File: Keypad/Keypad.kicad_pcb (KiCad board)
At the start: 2 copper layers, 41 parts, among them SW1 SW_Push, SW10 SW_Push, SW11 SW_Push, SW12 SW_Push, SW13 SW_Push, SW14 SW_Push, SW15 SW_Push, SW16 SW_Push, SW2 SW_Push, SW3 SW_Push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

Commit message: Working on de10lite keypad 2.0
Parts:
- removed R6_1K, R7_1K, R8_1K: R_Small_US, Resistor_THT:R_Axial_DIN0207_L6.3mm_D2.5mm_P7.62mm_Horizontal
- added R6_1K1: R_Small_US, Resistor_SMD:R_0603_1608Metric, F.Cu at (113.2, 66.5)
- added R7_1K1: R_Small_US, Resistor_SMD:R_0603_1608Metric, F.Cu at (113.2, 77.5)
- added R8_1K1: R_Small_US, Resistor_SMD:R_0603_1608Metric, F.Cu at (113.2, 87.8)
- D1, D10, D11, D12, D13, D14, D15, D16, D2, D3, D4, D5, D6, D7, D8, D9: footprint Diode_THT:D_A-405_P7.62mm_Horizontal -> Diode_SMD:D_SOD-123
- R1_330, R2_330, R3_330, R4_330: footprint Resistor_THT:R_Axial_DIN0207_L6.3mm_D2.5mm_P7.62mm_Horizontal -> Resistor_SMD:R_0603_1608Metric
- R5_1K1: renamed from R5_1K; footprint Resistor_THT:R_Axial_DIN0207_L6.3mm_D2.5mm_P7.62mm_Horizontal -> Resistor_SMD:R_0603_1608Metric
- SW1, SW10, SW11, SW12, SW13, SW14, SW15, SW16, SW2, SW3, SW4, SW5, SW6, SW7, SW8, SW9: footprint Resistor_THT:R_Axial_DIN0204_L3.6mm_D1.6mm_P5.08mm_Horizontal -> Button_Switch_SMD:SW_SPST_TL3305B
- moved D1 4.16 mm to (121.3, 57.4), turned to 180 degrees
- moved R5_1K1 4.10 mm to (113.2, 56.9)
- moved D4 4.00 mm to (121.3, 88.1), turned to 180 degrees
- moved D9 3.95 mm to (142.7, 57.4), turned to 180 degrees
- moved D11 3.91 mm to (143.1, 78.0), turned to 180 degrees
- moved D12 3.88 mm to (143.0, 88.1), turned to 180 degrees
- moved D8 3.88 mm to (132.2, 88.1), turned to 180 degrees
- moved D13 3.86 mm to (153.7, 57.5), turned to 180 degrees
- moved D2 3.84 mm to (121.4, 67.9), turned to 180 degrees
- moved D5 3.81 mm to (132.0, 57.4), turned to 180 degrees
- moved D3 3.79 mm to (121.3, 78.0), turned to 180 degrees
- moved D10 3.79 mm to (142.9, 67.9), turned to 180 degrees
- moved D14 3.79 mm to (153.7, 67.9), turned to 180 degrees
- moved D7 3.79 mm to (132.2, 78.0), turned to 180 degrees
- moved D16 3.75 mm to (153.7, 88.1), turned to 180 degrees
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- renumbered Keypad to U1
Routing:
- net Net-(SW13-Pad2): track 47.7 -> 90.1 mm, vias 0 -> 4
- net Net-(SW1-Pad2): track 58.4 -> 97.9 mm, vias 0 -> 4
- net Net-(SW10-Pad2): track 45.2 -> 82.3 mm, vias 0 -> 4
- net Net-(SW5-Pad2): track 52.5 -> 88.3 mm, vias 0 -> 4
- net Net-(D8-Pad1): track 5.11 -> 19.6 mm
- net Net-(D12-Pad1): track 5.10 -> 19.5 mm
- net Net-(D6-Pad1): track 5.30 -> 19.6 mm
- net Net-(D5-Pad1): track 5.38 -> 19.7 mm
- net Net-(D13-Pad1): track 5.54 -> 19.8 mm
- net Net-(D16-Pad1): track 5.05 -> 19.3 mm
- net Net-(D10-Pad1): track 5.38 -> 19.6 mm
- net Net-(D9-Pad1): track 5.44 -> 19.6 mm
- net Net-(D14-Pad1): track 5.48 -> 19.6 mm
- net Net-(D1-Pad1): track 5.18 -> 19.2 mm
- net Net-(D7-Pad1): track 5.63 -> 19.6 mm
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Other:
- board outline added: 54.1 x 54.1 mm
- copper layers 2 -> 4

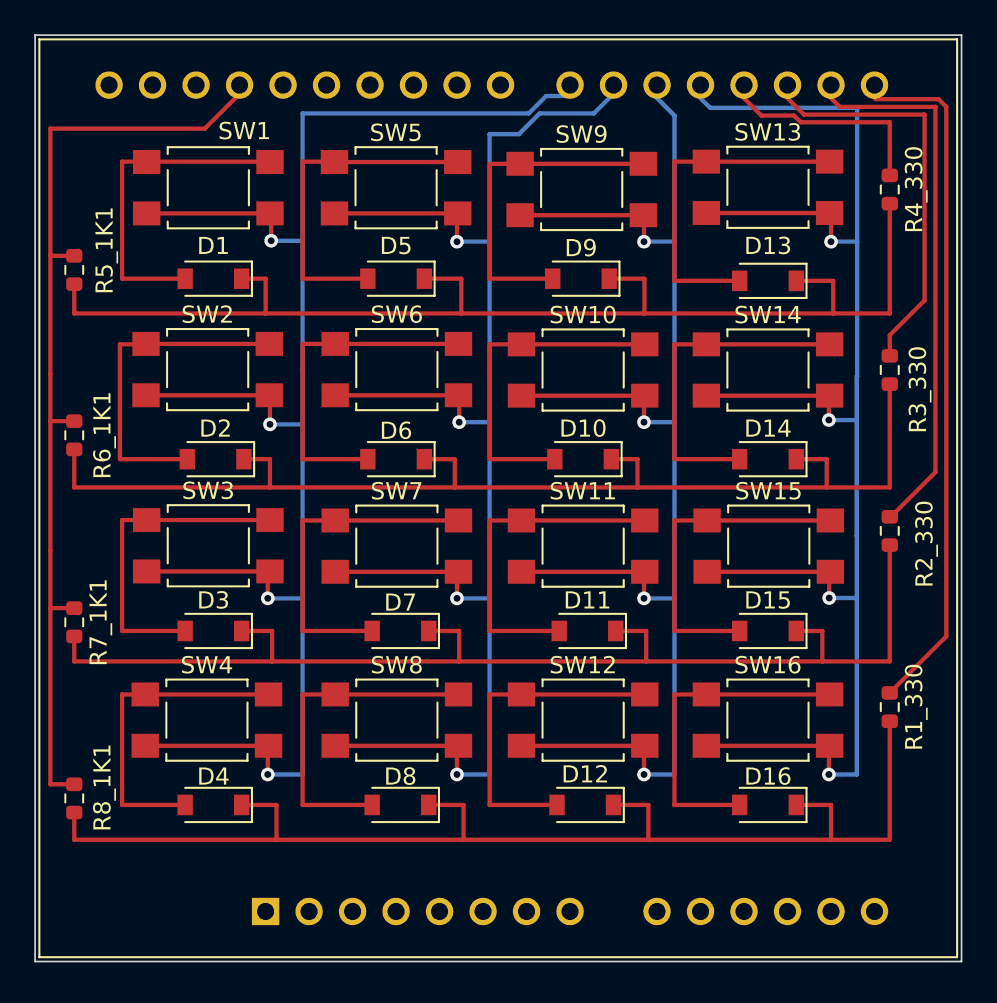
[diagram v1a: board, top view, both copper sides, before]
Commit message: Added in assembly and product files for PCBWay
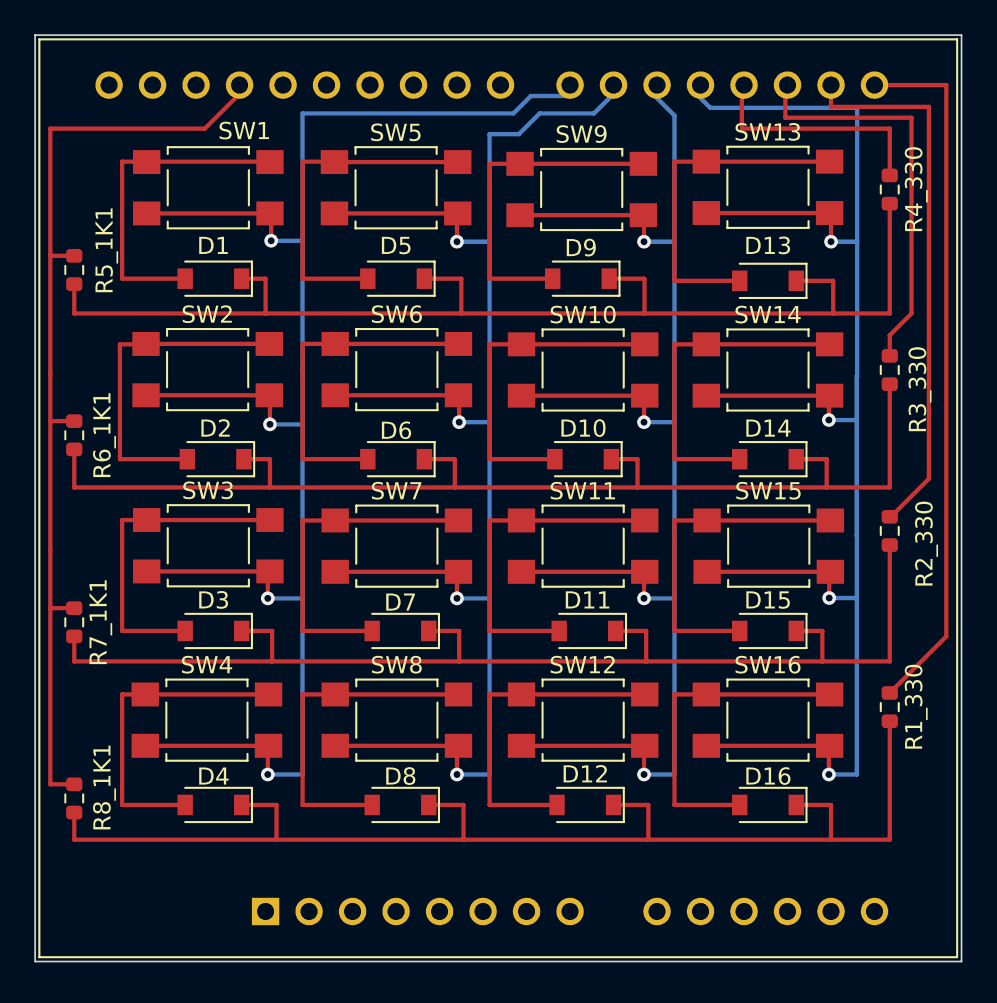
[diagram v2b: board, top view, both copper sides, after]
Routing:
- net Net-(R4_330-Pad1): track 12.3 -> 13.2 mm
- net Net-(R1_330-Pad1): track 40.2 -> 41.1 mm
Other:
- copper layers 4 -> 2
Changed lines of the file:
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@@
 (kicad_pcb (version 20211014) (generator pcbnew)
   (general
-    (thickness 4.69)
+    (thickness 1.6)
   )
   (paper "A4")
   (layers
     (0 "F.Cu" signal)
-    (1 "In1.Cu" signal)
-    (2 "In2.Cu" signal)
     (31 "B.Cu" signal)
     (32 "B.Adhes" user "B.Adhesive")
@@
       (layer "F.Cu" (type "copper") (thickness 0.035))
       (layer "dielectric 1" (type "core") (thickness 1.51) (material "FR4") (epsilon_r 4.5) (loss_tangent 0.02))
-      (layer "In1.Cu" (type "copper") (thickness 0.035))
-      (layer "dielectric 2" (type "prepreg") (thickness 1.51) (material "FR4") (epsilon_r 4.5) (loss_tangent 0.02))
-      (layer "In2.Cu" (type "copper") (thickness 0.035))
-      (layer "dielectric 3" (type "core") (thickness 1.51) (material "FR4") (epsilon_r 4.5) (loss_tangent 0.02))
       (layer "B.Cu" (type "copper") (thickness 0.035))
       (layer "B.Mask" (type "Bottom Solder Mask") (thickness 0.01))
@@
     (pad_to_mask_clearance 0)
     (pcbplotparams
-      (layerselection 0x0008020_ffffffff)
+      (layerselection 0x00010fc_ffffffff)
       (disableapertmacros false)
       (usegerberextensions false)
@@
   (segment (start 148.209 71.525) (end 150.114 71.525) (width 0.25) (layer "F.Cu") (net 29))
   (segment (start 148.209 77.978) (end 148.209 71.525) (width 0.25) (layer "F.Cu") (net 29))
+  (segment (start 159.893 46.101) (end 159.891 46.099) (width 0.25) (layer "F.Cu") (net 30))
   (segment (start 160.782 81.598) (end 164.084 78.296) (width 0.25) (layer "F.Cu") (net 30))
-  (segment (start 164.084 78.296) (end 164.084 47.371) (width 0.25) (layer "F.Cu") (net 30))
-  (segment (start 163.634 46.921) (end 159.951 46.921) (width 0.25) (layer "F.Cu") (net 30))
-  (segment (start 164.084 47.371) (end 163.634 46.921) (width 0.25) (layer "F.Cu") (net 30))
-  (segment (start 159.951 46.921) (end 159.766 46.736) (width 0.25) (layer "F.Cu") (net 30))
-  (segment (start 163.449 68.707) (end 163.449 47.372396) (width 0.25) (layer "F.Cu") (net 31))
-  (segment (start 160.782 71.374) (end 163.449 68.707) (width 0.25) (layer "F.Cu") (net 31))
-  (segment (start 157.861 47.371) (end 157.226 46.736) (width 0.25) (layer "F.Cu") (net 31))
-  (segment (start 163.449 47.372396) (end 163.447604 47.371) (width 0.25) (layer "F.Cu") (net 31))
-  (segment (start 163.447604 47.371) (end 157.861 47.371) (width 0.25) (layer "F.Cu") (net 31))
-  (segment (start 160.782 60.706) (end 162.814 58.674) (width 0.25) (layer "F.Cu") (net 32))
-  (segment (start 155.771 47.821) (end 154.686 46.736) (width 0.25) (layer "F.Cu") (net 32))
-  (segment (start 162.814 58.674) (end 162.814 47.821) (width 0.25) (layer "F.Cu") (net 32))
+  (segment (start 164.084 46.101) (end 159.893 46.101) (width 0.25) (layer "F.Cu") (net 30))
+  (segment (start 164.084 78.296) (end 164.084 46.101) (width 0.25) (layer "F.Cu") (net 30))
+  (segment (start 163.068 69.088) (end 163.068 47.371) (width 0.25) (layer "F.Cu") (net 31))
+  (segment (start 157.353 47.371) (end 157.351 47.369) (width 0.25) (layer "F.Cu") (net 31))
+  (segment (start 157.351 47.369) (end 157.351 46.099) (width 0.25) (layer "F.Cu") (net 31))
+  (segment (start 163.068 47.371) (end 157.353 47.371) (width 0.25) (layer "F.Cu") (net 31))
+  (segment (start 160.782 71.374) (end 163.068 69.088) (width 0.25) (layer "F.Cu") (net 31))
+  (segment (start 162.052 59.436) (end 162.052 48.006) (width 0.25) (layer "F.Cu") (net 32))
   (segment (start 160.782 61.976) (end 160.782 60.706) (width 0.25) (layer "F.Cu") (net 32))
-  (segment (start 162.814 47.821) (end 155.771 47.821) (width 0.25) (layer "F.Cu") (net 32))
-  (segment (start 155.584604 48.271) (end 155.192604 47.879) (width 0.25) (layer "F.Cu") (net 33))
-  (segment (start 153.289 47.879) (end 152.146 46.736) (width 0.25) (layer "F.Cu") (net 33))
-  (segment (start 160.782 51.308) (end 160.782 48.271) (width 0.25) (layer "F.Cu") (net 33))
-  (segment (start 160.782 48.271) (end 155.584604 48.271) (width 0.25) (layer "F.Cu") (net 33))
-  (segment (start 155.192604 47.879) (end 153.289 47.879) (width 0.25) (layer "F.Cu") (net 33))
+  (segment (start 162.052 48.006) (end 154.686 48.006) (width 0.25) (layer "F.Cu") (net 32))
+  (segment (start 154.686 48.006) (end 154.686 46.736) (width 0.25) (layer "F.Cu") (net 32))
+  (segment (start 160.782 60.706) (end 162.052 59.436) (width 0.25) (layer "F.Cu") (net 32))
+  (segment (start 152.146 48.641) (end 152.146 46.736) (width 0.25) (layer "F.Cu") (net 33))
+  (segment (start 160.782 48.641) (end 152.146 48.641) (width 0.25) (layer "F.Cu") (net 33))
+  (segment (start 160.782 51.308) (end 160.782 48.641) (width 0.25) (layer "F.Cu") (net 33))
   (segment (start 111.76 86.932) (end 113.157 86.932) (width 0.25) (layer "F.Cu") (net 34))
   (segment (start 111.76 76.645) (end 113.157 76.645) (width 0.25) (layer "F.Cu") (net 34))
@@
   (via (at 124.46 76.073) (size 0.8) (drill 0.4) (layers "F.Cu" "B.Cu") (net 35))
   (via (at 124.46 86.36) (size 0.8) (drill 0.4) (layers "F.Cu" "B.Cu") (net 35))
-  (segment (start 140.716 46.736) (end 139.7 47.752) (width 0.25) (layer "B.Cu") (net 35))
   (segment (start 126.492 76.073) (end 124.46 76.073) (width 0.25) (layer "B.Cu") (net 35))
-  (segment (start 126.492 55.118) (end 126.4216 55.1884) (width 0.25) (layer "B.Cu") (net 35))
   (segment (start 126.492 55.2588) (end 126.492 62.738) (width 0.25) (layer "B.Cu") (net 35))
   (segment (start 126.4216 55.1884) (end 126.492 55.2588) (width 0.25) (layer "B.Cu") (net 35))
+  (segment (start 141.986 46.736) (end 139.827 46.736) (width 0.25) (layer "B.Cu") (net 35))
   (segment (start 126.492 76.073) (end 126.492 86.36) (width 0.25) (layer "B.Cu") (net 35))
   (segment (start 126.492 65.913) (end 126.492 76.073) (width 0.25) (layer "B.Cu") (net 35))
+  (segment (start 126.492 47.752) (end 126.492 55.118) (width 0.25) (layer "B.Cu") (net 35))
+  (segment (start 126.492 55.118) (end 126.4216 55.1884) (width 0.25) (layer "B.Cu") (net 35))
+  (segment (start 139.827 46.736) (end 138.811 47.752) (width 0.25) (layer "B.Cu") (net 35))
+  (segment (start 138.811 47.752) (end 126.492 47.752) (width 0.25) (layer "B.Cu") (net 35))
   (segment (start 126.492 62.6248) (end 126.492 65.913) (width 0.25) (layer "B.Cu") (net 35))
-  (segment (start 141.986 46.736) (end 140.716 46.736) (width 0.25) (layer "B.Cu") (net 35))
   (segment (start 126.4216 55.1884) (end 124.6574 55.1884) (width 0.25) (layer "B.Cu") (net 35))
-  (segment (start 126.492 47.752) (end 126.492 55.118) (width 0.25) (layer "B.Cu") (net 35))
   (segment (start 126.492 86.36) (end 124.46 86.36) (width 0.25) (layer "B.Cu") (net 35))
-  (segment (start 139.7 47.752) (end 126.492 47.752) (width 0.25) (layer "B.Cu") (net 35))
   (segment (start 126.492 65.913) (end 124.587 65.913) (width 0.25) (layer "B.Cu") (net 35))
   (segment (start 148.209 57.531) (end 148.209 50.57) (width 0.25) (layer "F.Cu") (net 36))
